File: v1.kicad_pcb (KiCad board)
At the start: 2 copper layers, 65.1 x 65.2 mm, 73 parts, among them J1 Conn_01x04, J101 K1X06, J102 FTDI, J103 ISP, J2 Conn_01x04, J201 Conn_Coaxial, J3 Conn_01x04, J4 Conn_01x04, J5 Conn_01x04, Q1 AO3400A, SW101 SW_Push, U1 ATmega328P-AU, U201 CC1101RGPR, U3 PST61C24, U4 DS18B20, Y1 8MHz, Y201 26MHz

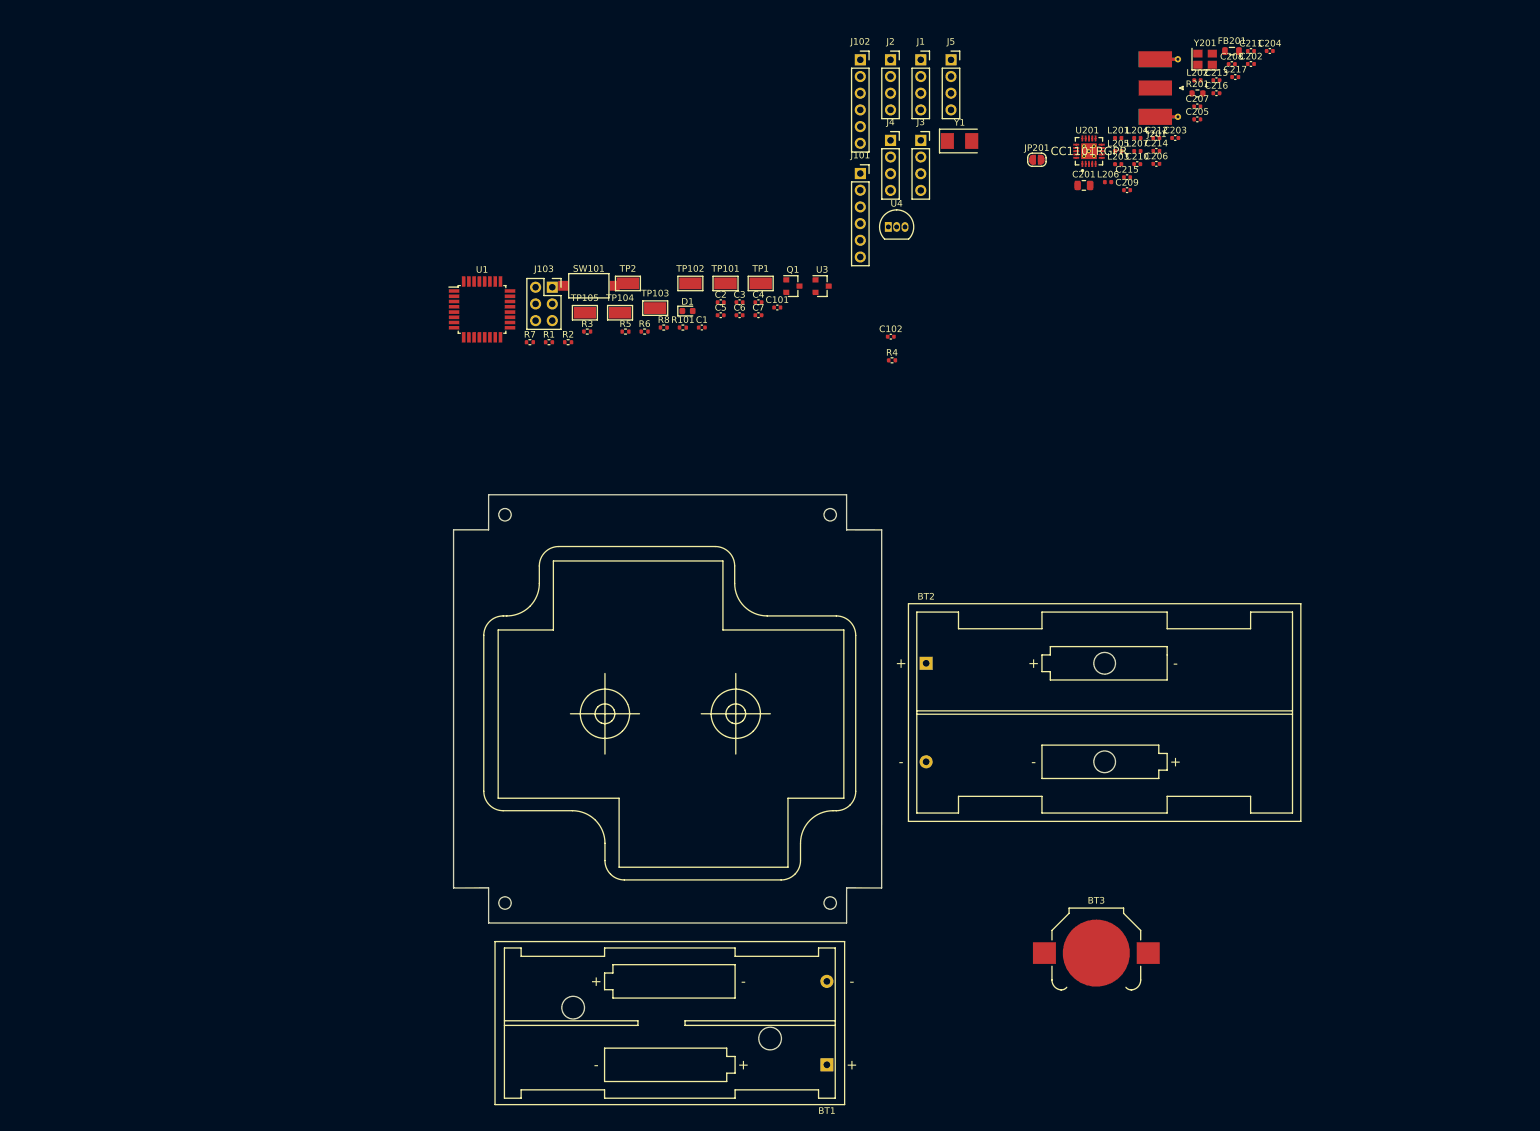
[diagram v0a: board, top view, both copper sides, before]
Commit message: select more JLC components
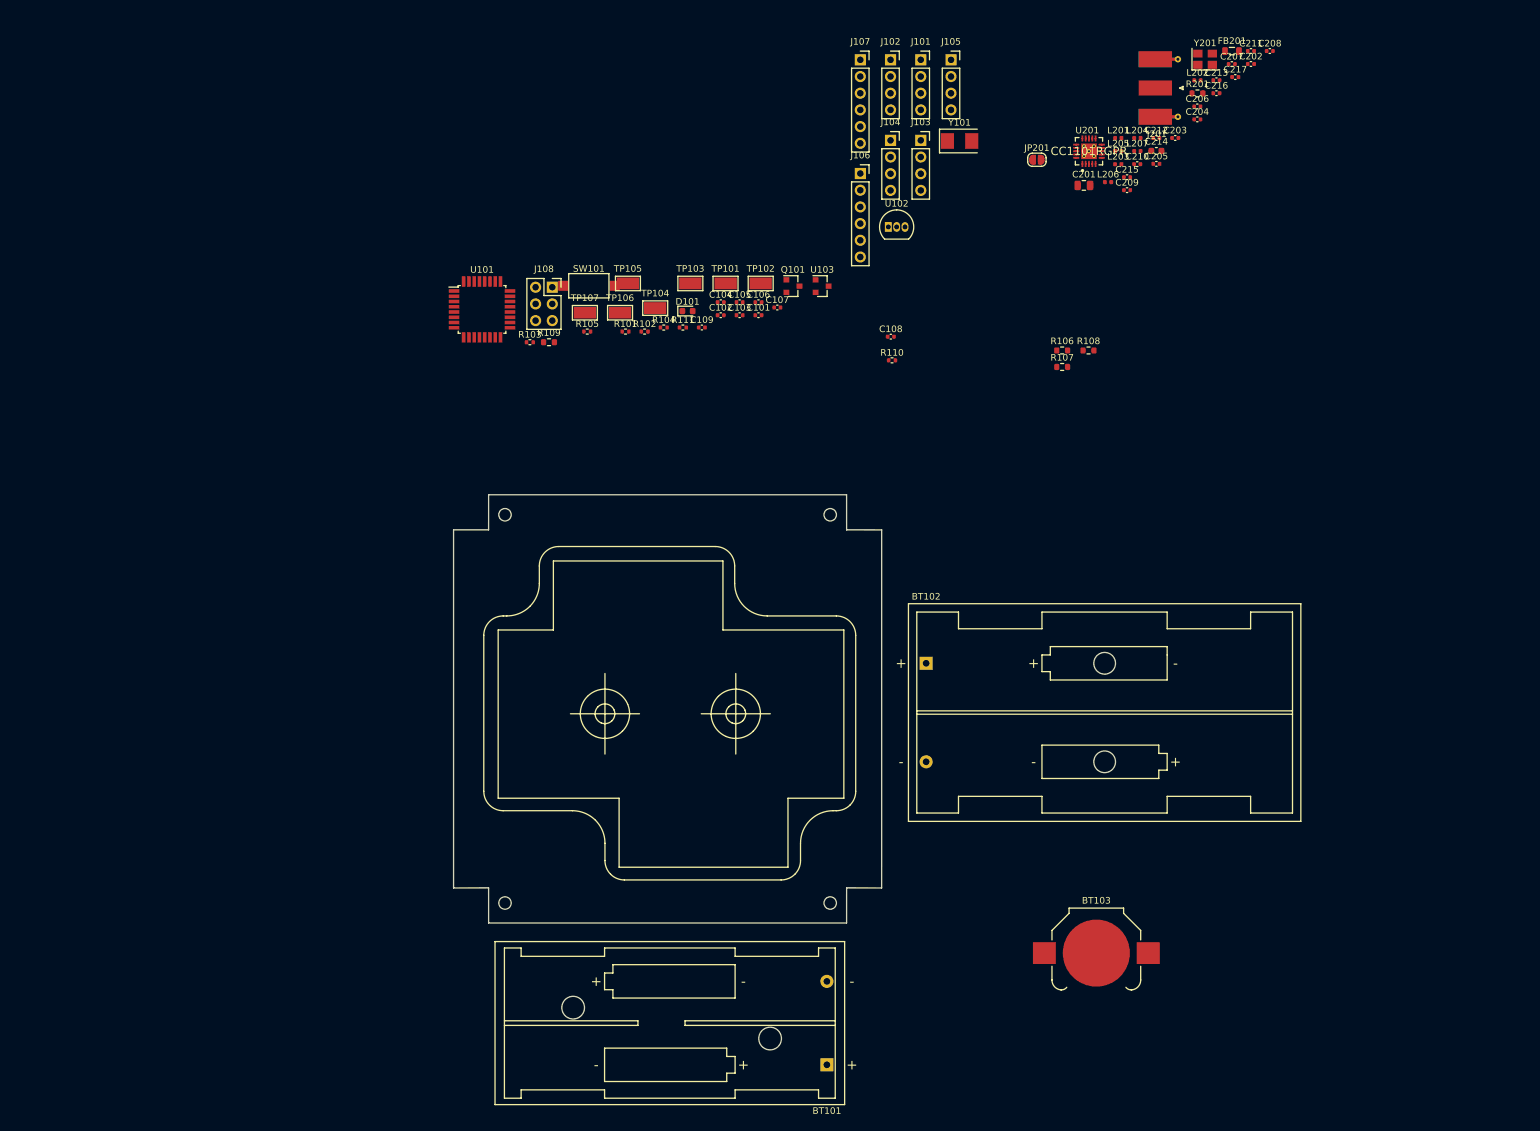
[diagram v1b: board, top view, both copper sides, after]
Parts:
- removed R2: 30, Resistor_SMD:R_0402_1005Metric
- added R106: 10, Resistor_SMD:R_0603_1608Metric, F.Cu at (244.3, 66.6)
- added R107: 10, Resistor_SMD:R_0603_1608Metric, F.Cu at (244.3, 69.1)
- added R108: 10, Resistor_SMD:R_0603_1608Metric, F.Cu at (248.3, 66.6)
- C214: footprint Capacitor_SMD:C_0402_1005Metric -> Capacitor_SMD:C_0603_1608Metric
- R103: renamed from R7; value 1.5k -> 10k
- R109: renamed from R1; footprint Resistor_SMD:R_0402_1005Metric -> Resistor_SMD:R_0603_1608Metric
- renumbered BT1 to BT101, BT2 to BT102, BT3 to BT103, C7 to C101, C5 to C102, C6 to C103, C2 to C104, C3 to C105, C4 to C106, C101 to C107, C102 to C108, C1 to C109, C205 to C204, C206 to C205, C207 to C206, C208 to C207, C204 to C208, D1 to D101, J1 to J101, J2 to J102, J3 to J103, J4 to J104, J5 to J105, J101 to J106, J102 to J107, J103 to J108, Q1 to Q101, R5 to R101, R6 to R102, R8 to R104, R3 to R105, R4 to R110, R101 to R111, TP1 to TP102, TP102 to TP103, TP103 to TP104, TP2 to TP105, TP104 to TP106, TP105 to TP107, U1 to U101, U4 to U102, U3 to U103, Y1 to Y101

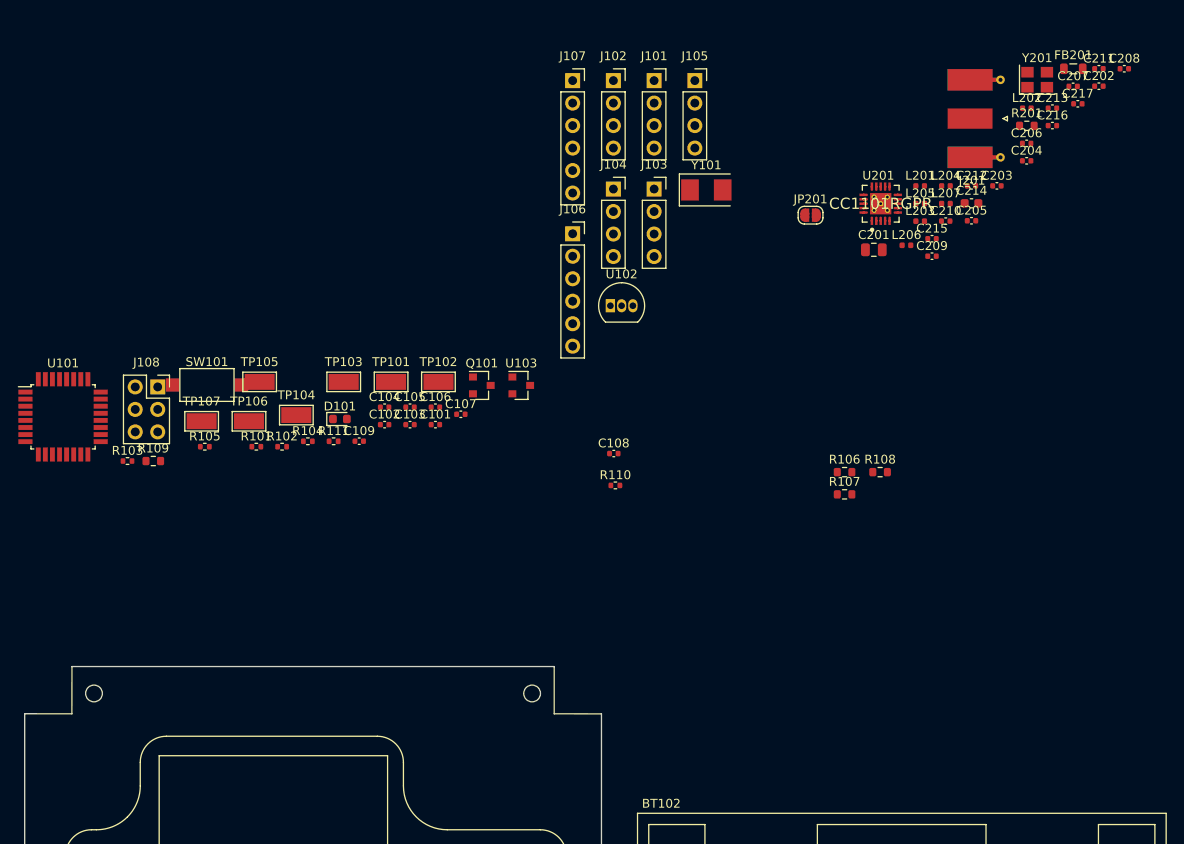
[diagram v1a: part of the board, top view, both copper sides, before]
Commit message: raw component placement
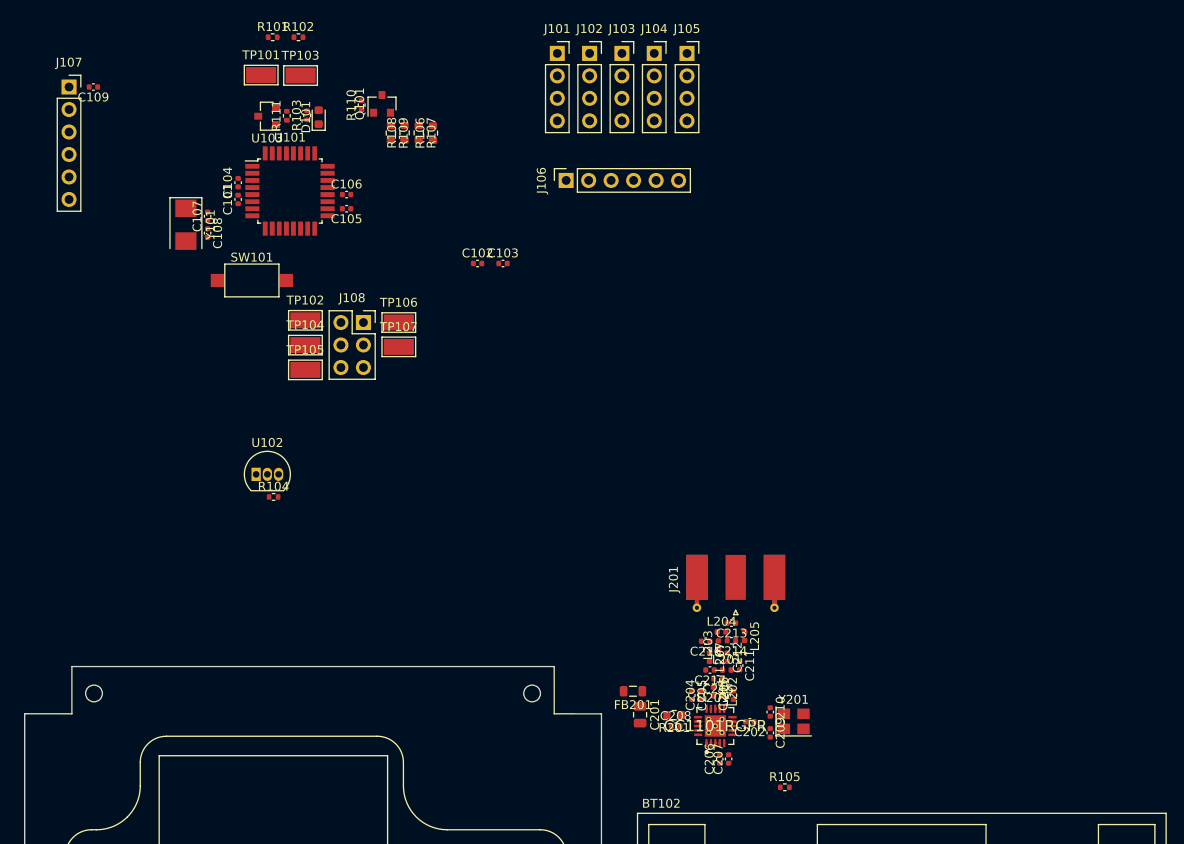
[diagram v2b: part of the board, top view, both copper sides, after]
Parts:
- removed JP201: AntGND, Jumper:SolderJumper-2_P1.3mm_Open_RoundedPad1.0x1.5mm
- C214: footprint Capacitor_SMD:C_0603_1608Metric -> Capacitor_SMD:C_0402_1005Metric
- moved C208 89.9 mm to (225.2, 95.3)
- moved FB201 86.1 mm to (220.4, 91.3), turned to 180 degrees
- moved C207 85.4 mm to (231.2, 99.0), turned to 90 degrees
- moved C202 81.9 mm to (233.6, 94.8), turned to 180 degrees
- moved C211 78.7 mm to (232.4, 88.5), turned to 270 degrees
- moved C206 77.7 mm to (230.2, 99.0), turned to 90 degrees
- moved R201 77.6 mm to (225.1, 94.0), turned to 180 degrees
- moved Y201 77.5 mm to (238.6, 94.8)
- moved C217 76.3 mm to (229.1, 89.0), turned to 180 degrees
- moved R105 76.0 mm to (237.6, 102.2)
- moved L202 74.3 mm to (230.5, 91.4), turned to 270 degrees
- moved C204 70.7 mm to (228.1, 91.8), turned to 90 degrees
- moved C216 70.2 mm to (228.6, 85.7), turned to 180 degrees
- moved C213 68.5 mm to (231.5, 83.7), turned to 180 degrees
- moved R108 66.0 mm to (194.6, 28.3), turned to 90 degrees
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- renumbered R107 to R106, R106 to R107
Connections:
- C201 pad 1: +3V0 -> VDD
- C202 pad 2: +3V0 -> VDD
- C203 pad 1: +3V0 -> VDD
- C204 pad 1: +3V0 -> VDD
- C205 pad 2: +3V0 -> VDD
- C206 pad 2: +3V0 -> VDD
- C208 pad 2: +3V0 -> VDD
- FB201 pad 1: +3V0 -> VDD
- J201 pad 2: Net-(J201-Pad2) -> GND
- L202 pad 2: /CC1101/RF_N -> /CC1101/RF_P
- L206 pad 2: /CC1101/RF_P -> /CC1101/RF_N
- U201 pad 11: +3V0 -> VDD
- U201 pad 14: +3V0 -> VDD
- U201 pad 15: +3V0 -> VDD
- U201 pad 18: +3V0 -> VDD
- U201 pad 4: +3V0 -> VDD
- U201 pad 9: +3V0 -> VDD

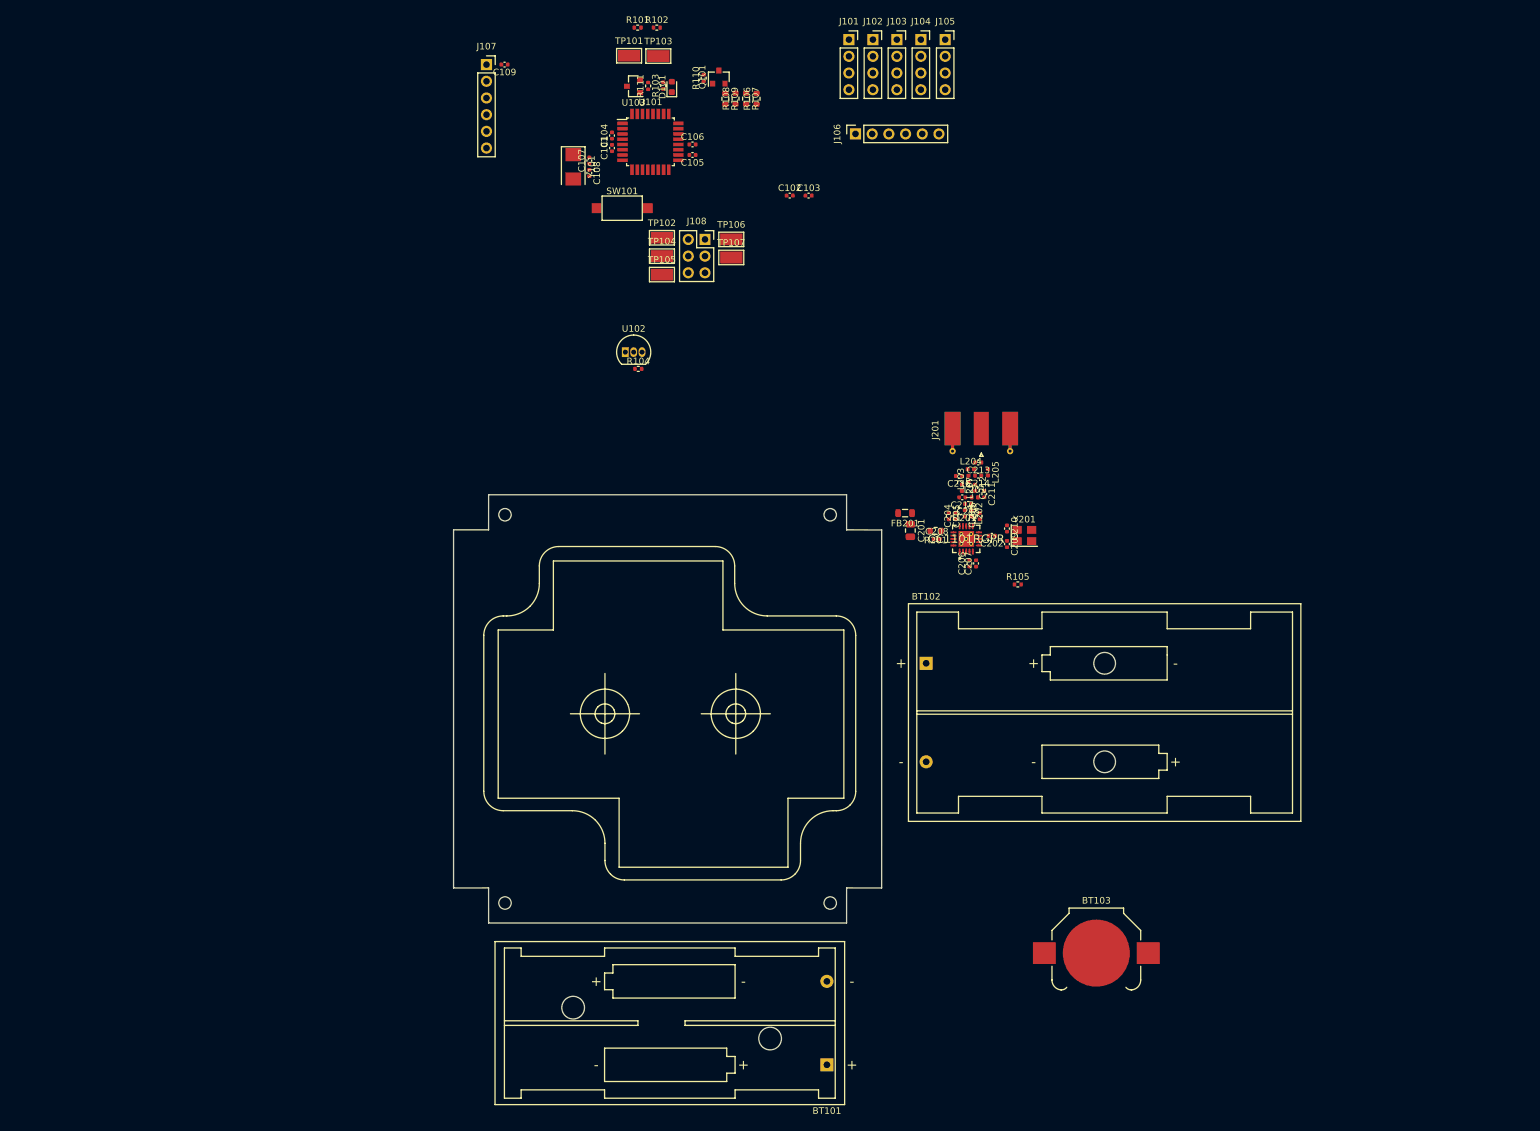
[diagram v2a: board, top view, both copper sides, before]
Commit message: place CC1101 circuits
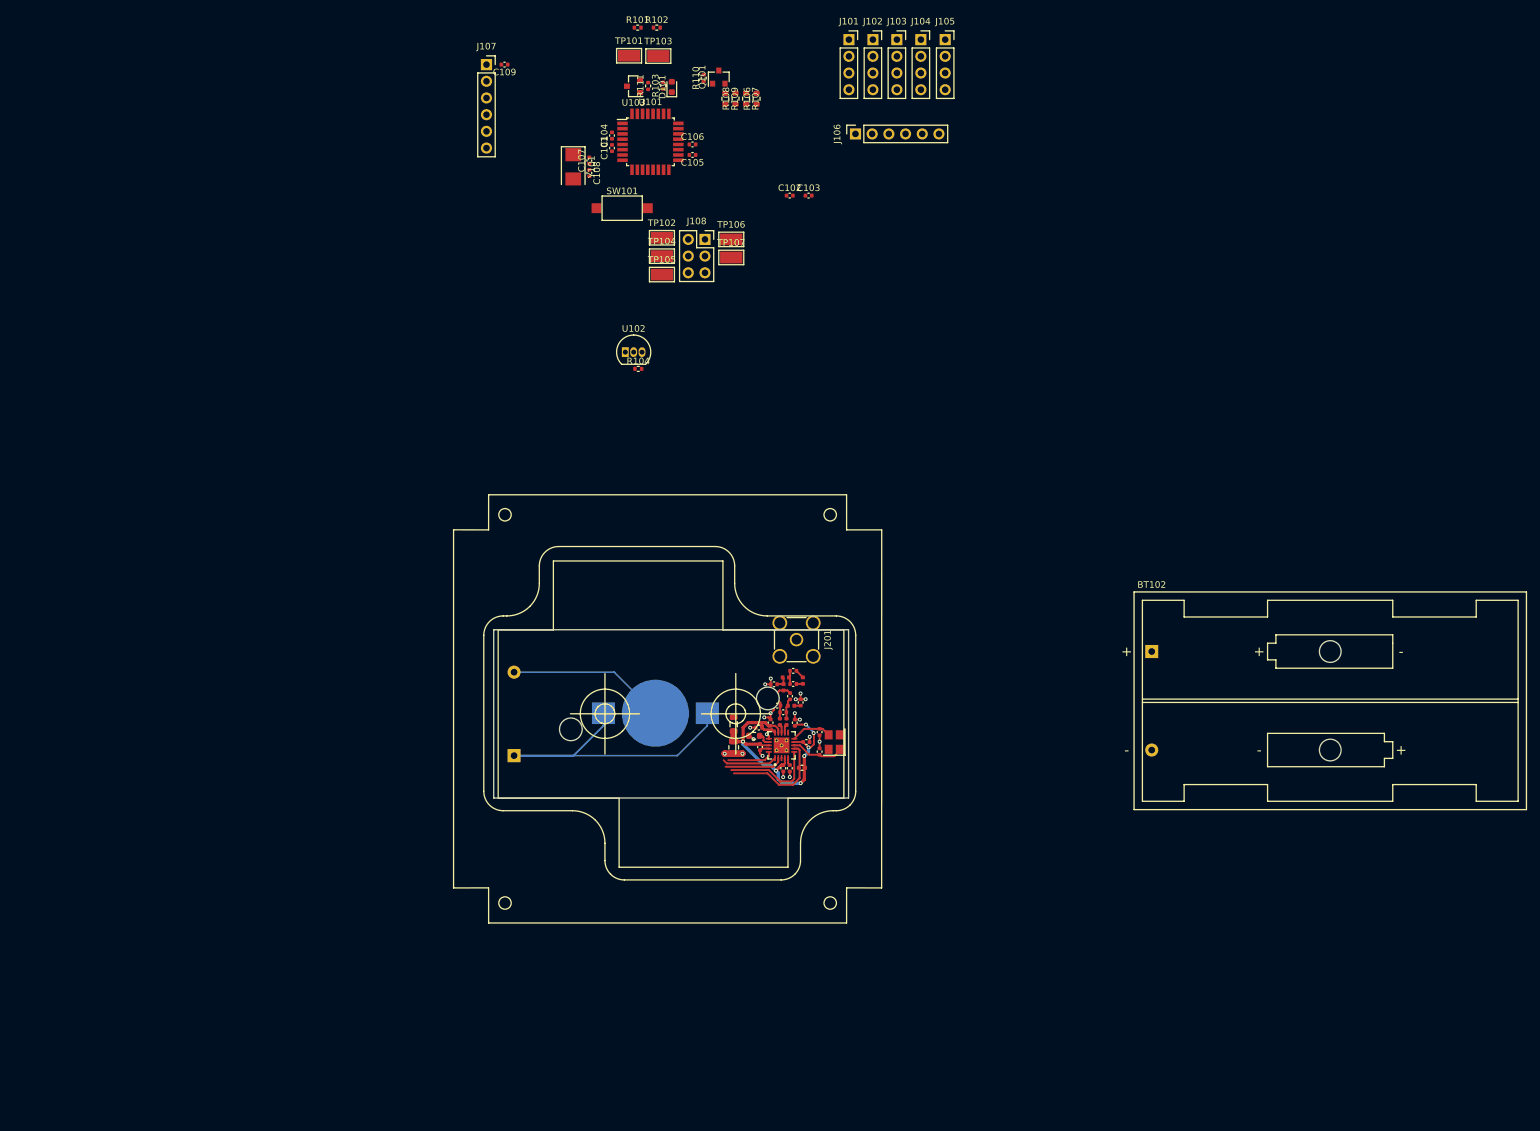
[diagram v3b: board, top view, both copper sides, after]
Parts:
- BT101, BT103: moved to B.Cu
- J201: footprint Connector_Coaxial:SMA_Molex_73251-1153_EdgeMount_Horizontal -> Connector_Coaxial:SMA_Amphenol_901-144_Vertical
- moved BT103 76.4 mm to (182.4, 121.8), turned to 180 degrees
- moved BT101 66.9 mm to (160.9, 128.2), turned to 0 degrees
- moved C205 43.2 mm to (198.2, 124.0), turned to 0 degrees
- moved R105 43.1 mm to (204.7, 130.1)
- moved Y201 42.7 mm to (209.6, 126.2), turned to 90 degrees
- moved C201 42.6 mm to (194.3, 127.0)
- moved C209 42.6 mm to (207.4, 127.6), turned to 90 degrees
- moved C212 42.4 mm to (202.9, 119.2)
- moved C215 42.4 mm to (201.8, 121.7)
- moved C216 42.4 mm to (200.4, 117.4)
- moved C217 42.4 mm to (200.9, 120.7)
- moved L207 42.4 mm to (200.9, 119.2)
- moved C213 42.4 mm to (203.4, 115.3)
- moved C214 42.4 mm to (203.4, 117.3)
- moved L202 42.4 mm to (202.3, 123.1)
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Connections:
- R105 pad 2: +3V0 -> VDD
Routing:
- net +3V0: track 0.00 -> 50.6 mm
- net VDD: track 0.00 -> 49.0 mm, vias 0 -> 7
- net GND: track 0.00 -> 47.5 mm, vias 0 -> 21
- net /D10: track 0.00 -> 16.5 mm
- net /D2: track 0.00 -> 14.6 mm
- net /MISO: track 0.00 -> 8.93 mm
- net /SCK: track 0.00 -> 8.34 mm
- net /CC1101/OSC1: track 0.00 -> 8.19 mm
- net /MOSI: track 0.00 -> 7.06 mm
- net /CC1101/OSC2: track 0.00 -> 6.24 mm
- net Net-(C215-Pad2): track 0.00 -> 3.18 mm
- net Net-(C212-Pad2): track 0.00 -> 3.17 mm
- net Net-(C212-Pad1): track 0.00 -> 2.31 mm
- net Net-(C213-Pad2): track 0.00 -> 2.13 mm
- net Net-(R201-Pad1): track 0.00 -> 2.12 mm
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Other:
- board size 65.1 x 65.2 mm -> 54 x 25.6 mm
